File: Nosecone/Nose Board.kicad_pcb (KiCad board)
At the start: 2 copper layers, 45.7 x 63.5 mm, 48 parts, among them J1 Conn_01x02, J2 Conn_02x04_Odd_Even, J3 Conn_02x03_Odd_Even, J4 Conn_Coaxial, J5 Conn_01x02, Q1 Q_PMOS_DGS, Q2 Q_PMOS_DGS, U1 RS485_converter_ISL83488, U10 MS5803-14BA, U11 MS5803-14BA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

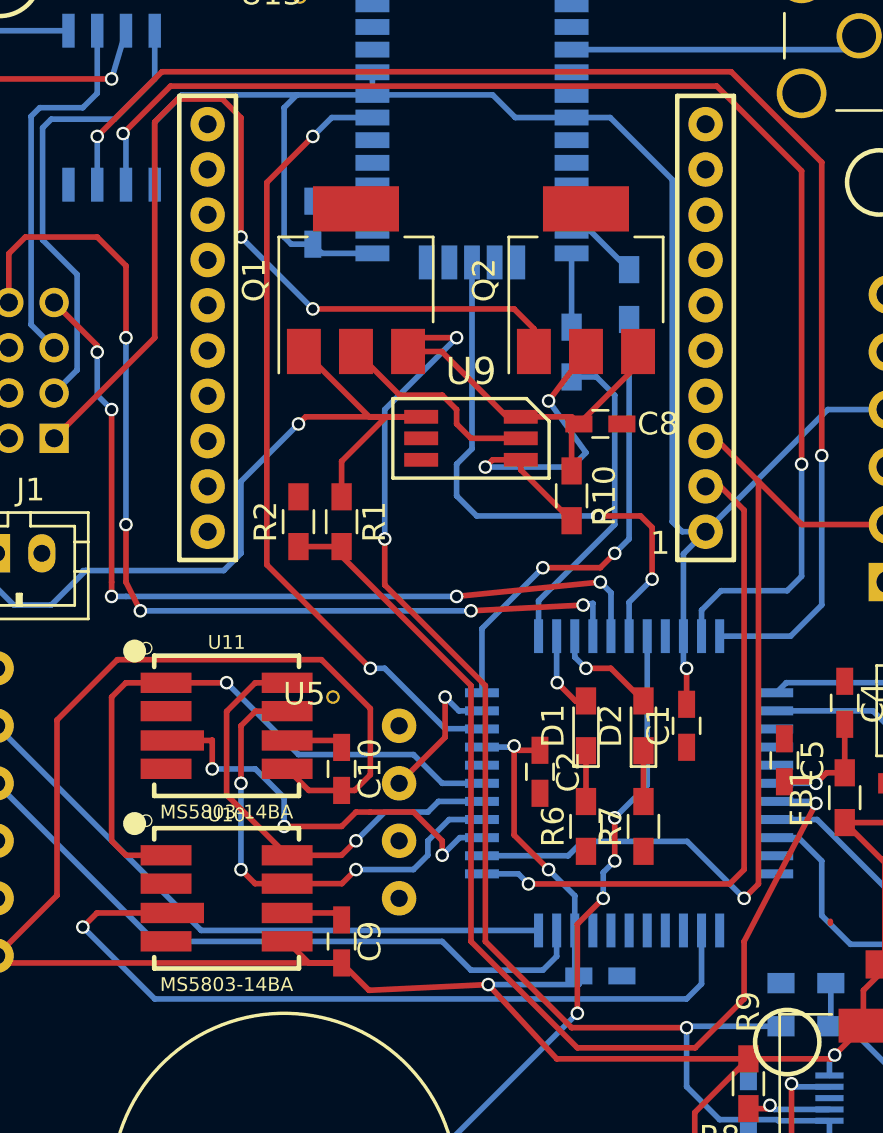
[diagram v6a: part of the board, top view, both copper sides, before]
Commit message: Actually fixed the DRC issues. Oops
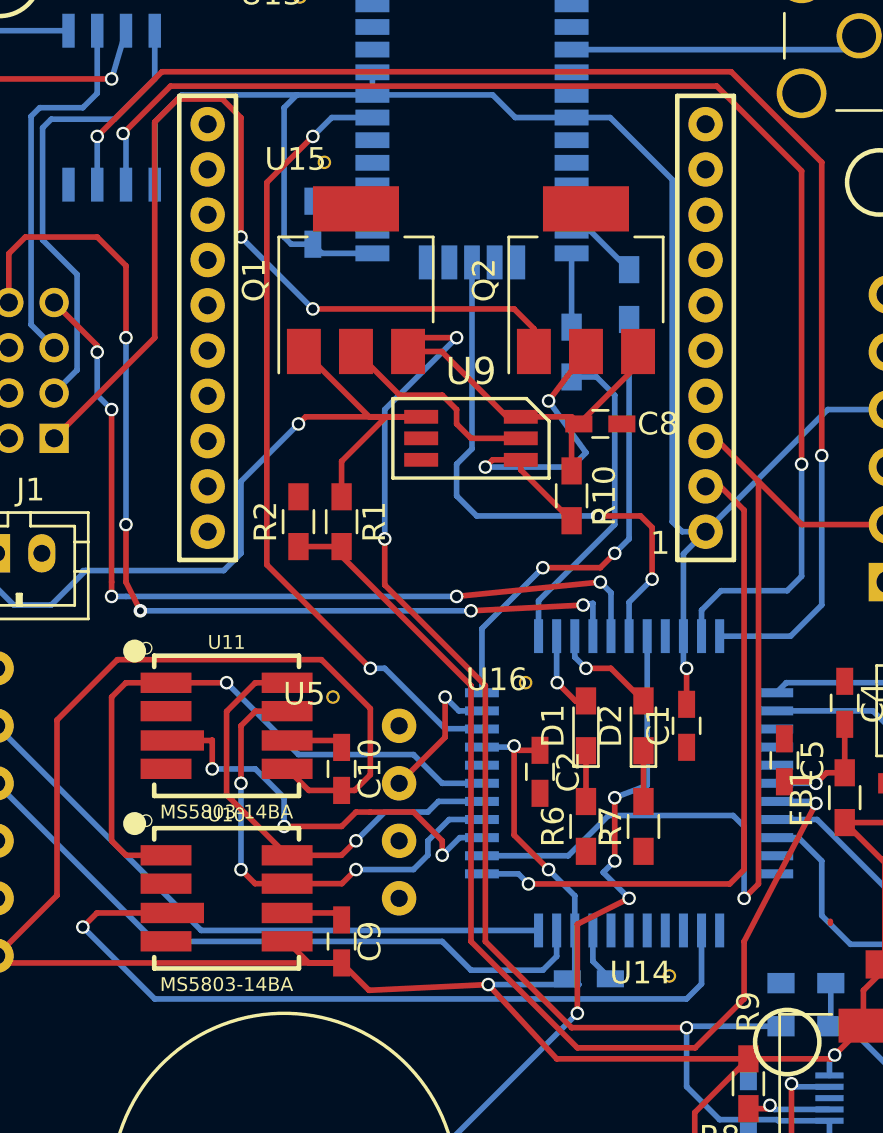
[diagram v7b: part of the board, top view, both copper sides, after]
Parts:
- added U14: Via-stitch, Misc components:Small-via, F.Cu at (165.6, 101.9)
- added U15: Via-stitch, Misc components:Small-via, F.Cu at (150.4, 65.9)
- added U16: Via-stitch, Misc components:Small-via, F.Cu at (159.3, 88.9)
- C8: value C -> 22uF
- R1: value R -> 90.9k
- R2: value R -> 10k
- R6, R7: value R -> 220
- moved C3 0.52 mm to (163.3, 102.6)
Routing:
- net /XBEE_Din: track 41.1 -> 43.9 mm
- net GND: track 5.07 -> 7.52 mm
- net /Buzzer_drive: track 30.2 -> 32.0 mm
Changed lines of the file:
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@@
 (kicad_pcb (version 4) (host pcbnew 4.0.7)
   (general
-    (links 149)
-    (no_connects 57)
-    (area 124.46 43.18 195.580001 142.240001)
+    (links 152)
+    (no_connects 2)
+    (area 134.544999 55.804999 180.415001 119.455001)
     (thickness 1.6)
     (drawings 8)
-    (tracks 484)
+    (tracks 487)
     (zones 0)
-    (modules 48)
+    (modules 51)
     (nets 48)
   )
@@
     (last_trace_width 0.25)
     (trace_clearance 0.18)
-    (zone_clearance 0.2)
+    (zone_clearance 0.18)
     (zone_45_only yes)
     (trace_min 0.18)
@@
     (pad_to_mask_clearance 0.2)
     (aux_axis_origin 0 0)
-    (grid_origin 160.02 91.44)
+    (grid_origin 167.767 100.711)
     (visible_elements 7FFEFFFF)
     (pcbplotparams
@@
       (effects (font (size 1 1) (thickness 0.15)))
     )
-    (fp_text value R (at 0 1.55 270) (layer F.Fab)
+    (fp_text value 90.9k (at 0 1.55 270) (layer F.Fab)
       (effects (font (size 1 1) (thickness 0.15)))
     )
@@
       (effects (font (size 1 1) (thickness 0.15)))
     )
-    (fp_text value R (at 0 1.55 90) (layer F.Fab)
+    (fp_text value 10k (at 0 1.55 90) (layer F.Fab)
       (effects (font (size 1 1) (thickness 0.15)))
     )
@@
   )
   (module Capacitors_SMD:C_0603_HandSoldering (layer B.Cu)
-    (at 163.83 102.489)
+    (at 163.322 102.616)
     (descr "Capacitor SMD 0603, hand soldering")
     (tags "capacitor 0603")
@@
       (effects (font (size 1 1) (thickness 0.15)))
     )
-    (fp_text value C (at 0 1.5) (layer F.Fab)
+    (fp_text value 22uF (at 0 1.5) (layer F.Fab)
       (effects (font (size 1 1) (thickness 0.15)))
     )
@@
       (effects (font (size 1 1) (thickness 0.15)))
     )
-    (fp_text value R (at 0 1.55 90) (layer F.Fab)
+    (fp_text value 220 (at 0 1.55 90) (layer F.Fab)
       (effects (font (size 1 1) (thickness 0.15)))
     )
@@
       (effects (font (size 1 1) (thickness 0.15)))
     )
-    (fp_text value R (at 0 1.55 90) (layer F.Fab)
+    (fp_text value 220 (at 0 1.55 90) (layer F.Fab)
       (effects (font (size 1 1) (thickness 0.15)))
     )
@@
     )
   )
+  (module "Misc components:Small-via" (layer F.Cu)
+    (at 165.608 101.854)
+    (fp_text reference U14 (at 0 0.5) (layer F.SilkS)
+      (effects (font (size 1 1) (thickness 0.15)))
+    )
+    (fp_text value Via-stitch (at 0 -0.5) (layer F.Fab)
+      (effects (font (size 1 1) (thickness 0.15)))
+    )
+    (pad 1 thru_hole circle (at 1.27 0.635) (size 0.6 0.6) (drill 0.4) (layers *.Cu *.Mask)
+      (net 2 GND))
+  )
+  (module "Misc components:Small-via" (layer F.Cu)
+    (at 150.368 65.913)
+    (fp_text reference U15 (at 0 0.5) (layer F.SilkS)
+      (effects (font (size 1 1) (thickness 0.15)))
+    )
+    (fp_text value Via-stitch (at 0 -0.5) (layer F.Fab)
+      (effects (font (size 1 1) (thickness 0.15)))
+    )
+    (pad 1 thru_hole circle (at 1.27 0.635) (size 0.6 0.6) (drill 0.4) (layers *.Cu *.Mask)
+      (net 2 GND))
+  )
+  (module "Misc components:Small-via" (layer F.Cu)
+    (at 159.258 88.9)
+    (fp_text reference U16 (at 0 0.5) (layer F.SilkS)
+      (effects (font (size 1 1) (thickness 0.15)))
+    )
+    (fp_text value Via-stitch (at 0 -0.5) (layer F.Fab)
+      (effects (font (size 1 1) (thickness 0.15)))
+    )
+    (pad 1 thru_hole circle (at 1.27 0.635) (size 0.6 0.6) (drill 0.4) (layers *.Cu *.Mask)
+      (net 2 GND))
+  )
   (gr_circle (center 176.149 67.437) (end 177.419 68.072) (layer F.SilkS) (width 0.2))
   (gr_line (start 134.62 119.38) (end 134.62 55.88) (angle 90) (layer Edge.Cuts) (width 0.15))
@@
   (segment (start 173.99 100.16) (end 173.99 100.076) (width 0.25) (layer F.Cu) (net 0))
   (segment (start 168.783 110.424) (end 168.783 110.744) (width 0.25) (layer B.Cu) (net 0))
-  (segment (start 137.16 83.82) (end 137.16 85.344) (width 0.25) (layer B.Cu) (net 1) (status 400000))
+  (segment (start 137.16 83.82) (end 137.16 85.344) (width 0.25) (layer B.Cu) (net 1))
   (segment (start 139.573 86.106) (end 141.097 84.582) (width 0.25) (layer B.Cu) (net 1))
   (segment (start 137.922 86.106) (end 139.573 86.106) (width 0.25) (layer B.Cu) (net 1))
@@
   (segment (start 155.915 77.79) (end 153.62 77.79) (width 0.25) (layer F.Cu) (net 1))
   (segment (start 153.62 77.79) (end 150.735 74.905) (width 0.25) (layer F.Cu) (net 1))
+  (segment (start 163.5 100.48) (end 163.5 101.844) (width 0.25) (layer B.Cu) (net 2))
+  (segment (start 163.5 101.844) (end 164.272 102.616) (width 0.25) (layer B.Cu) (net 2))
   (segment (start 149.99462 99.7077) (end 152.0927 99.7077) (width 0.25) (layer F.Cu) (net 2))
   (segment (start 152.0927 99.7077) (end 152.4 100.015) (width 0.25) (layer F.Cu) (net 2))
@@
   (segment (start 170.815 98.425) (end 170.18 99.06) (width 0.25) (layer F.Cu) (net 23))
   (via (at 170.18 99.06) (size 0.6) (drill 0.4) (layers F.Cu B.Cu) (net 23))
-  (segment (start 170.18 99.06) (end 167.665 96.545) (width 0.25) (layer B.Cu) (net 23))
-  (segment (start 167.665 96.545) (end 163.045 96.545) (width 0.25) (layer B.Cu) (net 23))
+  (segment (start 170.18 99.06) (end 170.18 95.885) (width 0.25) (layer B.Cu) (net 23))
+  (segment (start 170.18 95.885) (end 169.697 95.402) (width 0.25) (layer B.Cu) (net 23))
+  (segment (start 169.697 95.402) (end 164.188 95.402) (width 0.25) (layer B.Cu) (net 23))
   (segment (start 170.815 80.645) (end 169.03446 78.86446) (width 0.25) (layer F.Cu) (net 23))
-  (segment (start 162.41 97.18) (end 163.045 96.545) (width 0.25) (layer B.Cu) (net 23))
+  (segment (start 162.41 97.18) (end 164.188 95.402) (width 0.25) (layer B.Cu) (net 23))
   (segment (start 168.4782 78.86446) (end 169.03446 78.86446) (width 0.25) (layer F.Cu) (net 23))
   (segment (start 176.9505 108.3865) (end 177.8555 108.3865) (width 0.25) (layer B.Cu) (net 24))
@@
   (segment (start 141.605 69.85) (end 142.875 71.12) (width 0.25) (layer F.Cu) (net 44))
   (segment (start 138.43 69.85) (end 141.605 69.85) (width 0.25) (layer F.Cu) (net 44))
-  (via (at 143.51 86.36) (size 0.6) (drill 0.4) (layers F.Cu B.Cu) (net 44))
+  (via (at 143.51 86.36) (size 0.6) (drill 0.3) (layers F.Cu B.Cu) (net 44))
   (segment (start 137.7 70.58) (end 138.43 69.85) (width 0.25) (layer F.Cu) (net 44))
   (segment (start 143.51 86.36) (end 158.115 86.36) (width 0.25) (layer B.Cu) (net 44))
@@
   (via (at 162.814 104.14) (size 0.6) (drill 0.4) (layers F.Cu B.Cu) (net 45))
   (segment (start 162.814 100.203) (end 162.814 104.14) (width 0.25) (layer F.Cu) (net 45))
-  (segment (start 163.957 99.06) (end 162.814 100.203) (width 0.25) (layer F.Cu) (net 45))
-  (via (at 163.957 99.06) (size 0.6) (drill 0.4) (layers F.Cu B.Cu) (net 45))
-  (segment (start 163.957 97.917) (end 163.957 99.06) (width 0.25) (layer B.Cu) (net 45))
+  (segment (start 165.1 99.06) (end 162.814 100.203) (width 0.25) (layer F.Cu) (net 45))
+  (via (at 165.1 99.06) (size 0.6) (drill 0.4) (layers F.Cu B.Cu) (net 45))
+  (segment (start 163.957 97.917) (end 165.1 99.06) (width 0.25) (layer B.Cu) (net 45))
   (segment (start 164.465 97.409) (end 163.957 97.917) (width 0.25) (layer B.Cu) (net 45))
   (via (at 164.465 97.409) (size 0.6) (drill 0.4) (layers F.Cu B.Cu) (net 45))
-  (segment (start 164.465 95.504) (end 164.465 97.409) (width 0.25) (layer F.Cu) (net 45))
-  (via (at 164.465 95.504) (size 0.6) (drill 0.4) (layers F.Cu B.Cu) (net 45))
-  (segment (start 165.9 94.069) (end 164.465 95.504) (width 0.25) (layer B.Cu) (net 45))
+  (segment (start 164.465 94.615) (end 164.465 97.409) (width 0.25) (layer F.Cu) (net 45))
+  (via (at 164.465 94.615) (size 0.6) (drill 0.4) (layers F.Cu B.Cu) (net 45))
+  (segment (start 165.9 94.069) (end 164.465 94.615) (width 0.25) (layer B.Cu) (net 45))
   (segment (start 171.6 95.58) (end 173.406 95.58) (width 0.25) (layer B.Cu) (net 46))
   (segment (start 176.022 114.427) (end 162.052 114.427) (width 0.25) (layer B.Cu) (net 46))
@@
   (segment (start 172.58 96.38) (end 173.609 97.409) (width 0.25) (layer B.Cu) (net 47))
   (zone (net 2) (net_name GND) (layer B.Cu) (hatch edge 0.508)
-    (connect_pads (clearance 0.2))
-    (min_thickness 0.2)
-    (fill (arc_segments 16) (thermal_gap 0.508) (thermal_bridge_width 0.508))
+    (connect_pads (clearance 0.18))
+    (min_thickness 0.18)
+    (fill yes (arc_segments 16) (thermal_gap 0.508) (thermal_bridge_width 0.508))
     (polygon
       (pts
@@
   )
   (zone (net 2) (net_name GND) (layer F.Cu) (hatch edge 0.508)
-    (connect_pads (clearance 0.2))
-    (min_thickness 0.2)
-    (fill (arc_segments 16) (thermal_gap 0.508) (thermal_bridge_width 0.508))
+    (connect_pads (clearance 0.18))
+    (min_thickness 0.18)
+    (fill yes (arc_segments 16) (thermal_gap 0.508) (thermal_bridge_width 0.508))
     (polygon
       (pts

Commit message: Better routing
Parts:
- added ?: Via-stitch, Misc components:4_40_through_hole, F.Cu at (173.9, 65.4)
- added ?: Via-stitch, Misc components:4_40_through_hole, F.Cu at (137.3, 56.0)
- added ?: Via-stitch, Misc components:4_40_through_hole, F.Cu at (175.4, 112.9)
- added U17: Via-stitch, Misc components:4_40_through_hole, F.Cu at (138.3, 113.2)
- U6 (XBee): renamed from U6
- moved J5 4.54 mm to (163.4, 110.1), turned to 180 degrees
- moved BZ1 1.66 mm to (149.0, 110.4)
- moved ? 0.64 mm to (158.9, 88.4)
- moved D1 0.52 mm to (162.7, 91.6)
- moved R6 0.51 mm to (162.7, 95.8)
- renumbered U12 to ?, U13 to ?, U15 to ?, U16 to ?
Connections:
- net Net-(J2-Pad3) renamed /RS422out+
- J2 pad 4: Net-(J2-Pad4) -> /RS422in-
- J2 pad 5: Net-(J2-Pad5) -> /RS422out-
- J2 pad 6: Net-(J2-Pad6) -> /RS422in+
- J3 pad 3: (no net) -> Net-(J3-Pad3)
- J3 pad 4: (no net) -> Net-(J3-Pad4)
- U1 pad 5: Net-(J2-Pad6) -> /RS422in-
- U1 pad 6: Net-(J2-Pad5) -> /RS422in+
- U1 pad 7: Net-(J2-Pad4) -> /RS422out-
- U2 pad 1: (no net) -> Net-(U2-Pad1)
- U2 pad 3: (no net) -> Net-(U2-Pad3)
- U2 pad 36: (no net) -> Net-(U2-Pad36)
- U2 pad 37: (no net) -> Net-(U2-Pad37)
- U2 pad 4: (no net) -> Net-(U2-Pad4)
- U2 pad 43: (no net) -> Net-(U2-Pad43)
- U2 pad 44: (no net) -> Net-(U2-Pad44)
- U2 pad 5: (no net) -> Net-(U2-Pad5)
- U2 pad 6: (no net) -> Net-(U2-Pad6)
- U2 pad 7: (no net) -> Net-(U2-Pad7)
- U4 pad 16: (no net) -> Net-(U4-Pad16)
- U4 pad 2: (no net) -> Net-(U4-Pad2)
- U4 pad 23: (no net) -> Net-(U4-Pad23)
- U4 pad 24: (no net) -> Net-(U4-Pad24)
- U4 pad 28: (no net) -> Net-(U4-Pad28)
- U4 pad 3: (no net) -> Net-(U4-Pad3)
- U4 pad 30: (no net) -> Net-(U4-Pad30)
- U4 pad 6: (no net) -> Net-(U4-Pad6)
- U6 (XBee) pad 11: (no net) -> Net-(U6-Pad11)
- U6 (XBee) pad 12: (no net) -> Net-(U6-Pad12)
- U6 (XBee) pad 13: (no net) -> Net-(U6-Pad13)
- U6 (XBee) pad 14: (no net) -> Net-(U6-Pad14)
- U6 (XBee) pad 15: (no net) -> Net-(U6-Pad15)
- U6 (XBee) pad 16: (no net) -> Net-(U6-Pad16)
- U6 (XBee) pad 17: (no net) -> Net-(U6-Pad17)
- U6 (XBee) pad 18: (no net) -> Net-(U6-Pad18)
- U6 (XBee) pad 19: (no net) -> Net-(U6-Pad19)
- U6 (XBee) pad 20: (no net) -> Net-(U6-Pad20)
- U6 (XBee) pad 4: (no net) -> Net-(U6-Pad4)
- U6 (XBee) pad 5: (no net) -> Net-(U6-Pad5)
- U6 (XBee) pad 6: (no net) -> Net-(U6-Pad6)
- U6 (XBee) pad 7: (no net) -> Net-(U6-Pad7)
- U6 (XBee) pad 8: (no net) -> Net-(U6-Pad8)
- U6 (XBee) pad 9: (no net) -> Net-(U6-Pad9)
- U7 pad 1: (no net) -> Net-(U7-Pad1)
- U7 pad 3: (no net) -> Net-(U7-Pad3)
- U8 pad 10: (no net) -> Net-(U8-Pad10)
- U8 pad 2: (no net) -> Net-(U8-Pad2)
- U8 pad 6: (no net) -> Net-(U8-Pad6)
- U8 pad 7: (no net) -> Net-(U8-Pad7)
- U8 pad 9: (no net) -> Net-(U8-Pad9)
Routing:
- net Net-(J2-Pad4): track 23.2 -> 0.00 mm, vias 1 -> 0
- net /RS422in-: track 0.00 -> 19.5 mm
- net Net-(J2-Pad6): track 19.2 -> 0.00 mm
- net /RS422in+: track 0.00 -> 18.2 mm
- net /RS422out-: track 0.00 -> 17.1 mm
- net Net-(J2-Pad5): track 16.8 -> 0.00 mm
- net /XBEE_Din: track 43.9 -> 36.0 mm
- net VDC: track 83.6 -> 77.3 mm
- net /Vbatt_meas: track 47.8 -> 53.3 mm
- net /A2: track 41.7 -> 37.6 mm
- net Net-(Q2-Pad2): track 15.6 -> 11.5 mm
- net +3V3: track 227.7 -> 223.8 mm
- net /Debug_RX: track 45.0 -> 41.6 mm
- net /P2_CS: track 35.5 -> 32.1 mm
- net /Center_Din: track 61.6 -> 58.2 mm
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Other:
- net class differential added: clearance 0.19, trace_width 0.26, via_dia 0.6, via_drill 0.3
